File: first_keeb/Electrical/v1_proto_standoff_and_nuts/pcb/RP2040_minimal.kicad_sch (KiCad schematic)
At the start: 75 parts, among them J1 Conn_01x04_Socket, J2 Conn_01x04_Socket, P1 USB-TYPE-C-016, Q1 SN74LV1T34DBV, SW1 SK-3296S-01-L3, SW2 MS-22C01-G010, SW3 TS-1187A-B-A-B, SW4 MS-22C01-G010, SW5 TS-1187A-B-A-B, SW6 BUTT1, SW7 BUTT3, SW8 BUTT2, U1 AMS1117-2.5, U2 ME6208A44M3G, U3 PRTR5V0U2X, U4 MCP6001-OT, U5 STM32F401RCTx, U6 MCP6001-OT, U7 SLSS49E, U8 SLSS49E, U9 SLSS49E, Y1 8MHz

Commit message: - no more tan caps - adds 1u before ferrite - ties ties other side of boot0 resistor to gnd
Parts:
- removed J2: Conn_01x04_Socket, Connector_PinSocket_2.54mm:PinSocket_1x04_P2.54mm_Vertical, symbol Connector:Conn_01x04_Socket
- added C1: 1u, Capacitor_SMD:C_0402_1005Metric, symbol Device:C_Small
- C10: renamed from C9; value 10u -> 22u
- C11: renamed from C10; value 10u -> 22u
- C12: renamed from C11; value 10u -> 22u
- C13: renamed from C12; value 10u -> 22u
- C17: renamed from C16; value 4.7u -> 4u7
- U1: value AMS1117-2.5 -> ME6206A25XG; footprint Package_TO_SOT_SMD:SOT-223-3_TabPin2 -> Package_TO_SOT_SMD:SOT-23
- U2: footprint Package_TO_SOT_SMD:SOT-23 -> Package_TO_SOT_SMD:SOT-23-3
- renumbered C13 to C14, C14 to C15, C15 to C16, C17 to C18, C18 to C19, C1 to C2, C19 to C20, C20 to C21, C21 to C22, C22 to C23, C23 to C24, C24 to C25, C25 to C26, C26 to C27, C27 to C28, C28 to C29, C2 to C3, C29 to C30, C30 to C31, C31 to C32, C32 to C33, C3 to C4, C4 to C5, C5 to C6, C6 to C7, C7 to C8, C8 to C9
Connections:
- net BOOT0: now also R3.1, SW3.1; no longer R3.2
- net GND: now also R3.2, C1.2
- net VDD: now also C1.1
- net USART1_RX: no longer names the net of U5.59 (PB7)
- net USART1_TX: no longer names the net of U5.58 (PB6)
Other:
- note removed: "4.7u ceramic capacitor must be connected to one of the VDD pins"
- note removed: "Reccomend tantalum cap for improved stability on power supplies. To be cost effective, put the tantalum caps on MCU power first since the ADC uses that as its VREF and that requires more stability than the sensors"
- moved on the sheet: C2, C3, C4, C5, C6, C7, C8, C9, FB1, R3, R4

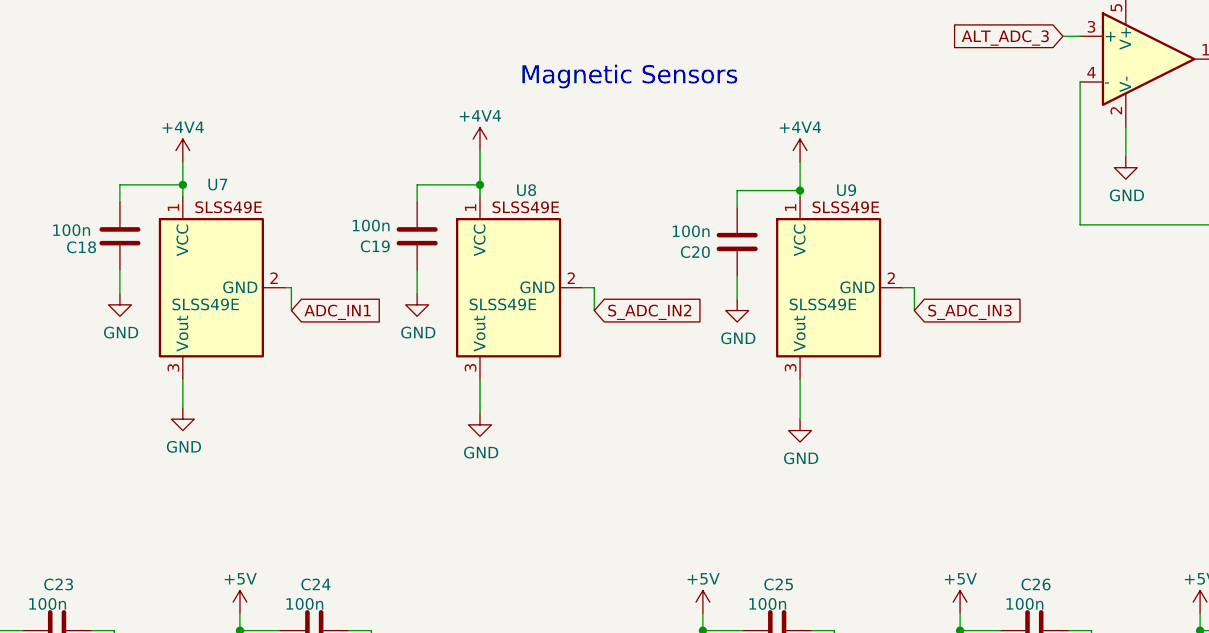
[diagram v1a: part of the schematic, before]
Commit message: fix mag sensor schematic
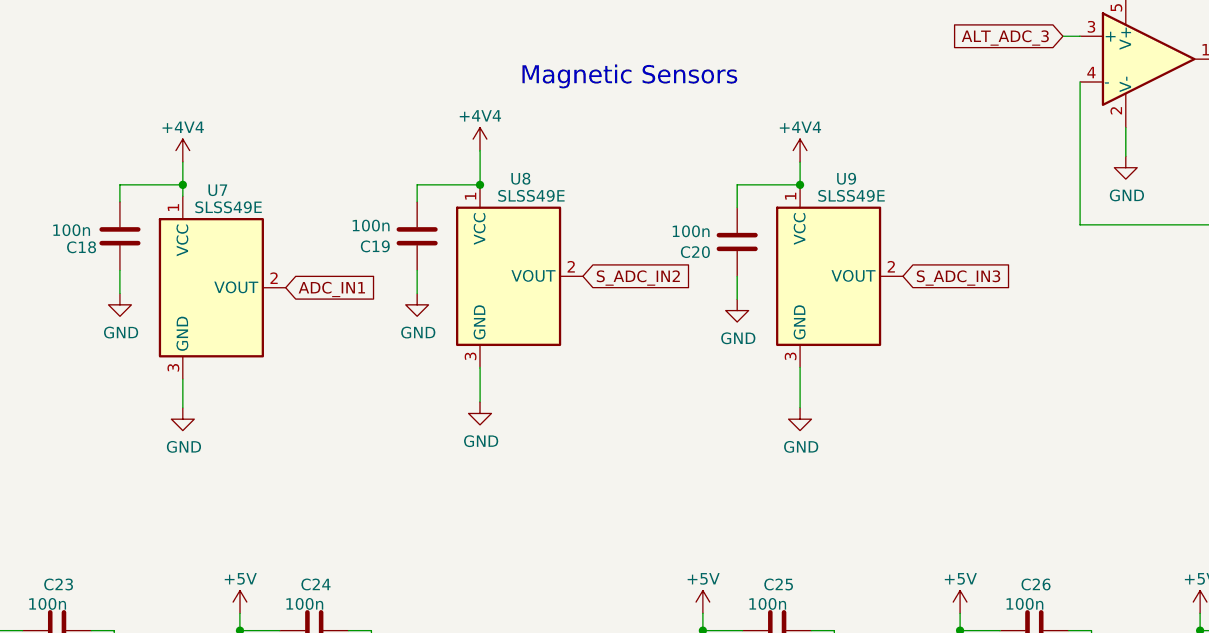
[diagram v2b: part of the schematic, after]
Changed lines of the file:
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@@
   (junction (at 236.22 46.355) (diameter 0) (color 0 0 0 0)
   )
-  (junction (at 330.2 167.64) (diameter 0) (color 0 0 0 0)
-  )
   (junction (at 101.6 40.64) (diameter 0) (color 0 0 0 0)
   )
@@
   (junction (at 73.025 40.64) (diameter 0) (color 0 0 0 0)
   )
+  (junction (at 330.2 167.005) (diameter 0) (color 0 0 0 0)
+  )
   (junction (at 41.275 66.04) (diameter 0) (color 0 0 0 0)
   )
@@
     (stroke (width 0) (type default))
   )
-  (wire (pts (xy 330.2 167.64) (xy 323.215 167.64))
-    (stroke (width 0) (type default))
-  )
   (wire (pts (xy 361.315 171.45) (xy 361.315 155.575))
     (stroke (width 0) (type default))
@@
     (stroke (width 0) (type default))
   )
-  (wire (pts (xy 273.05 178.435) (xy 273.685 178.435))
-    (stroke (width 0) (type default))
-  )
   (wire (pts (xy 228.6 134.62) (xy 228.6 133.985))
     (stroke (width 0) (type default))
@@
     (stroke (width 0) (type default))
   )
+  (wire (pts (xy 261.62 168.275) (xy 261.62 167.005))
+    (stroke (width 0) (type default))
+  )
   (wire (pts (xy 278.13 251.46) (xy 278.13 253.365))
     (stroke (width 0) (type default))
@@
     (stroke (width 0) (type default))
   )
+  (wire (pts (xy 330.2 164.465) (xy 330.2 167.005))
+    (stroke (width 0) (type default))
+  )
   (wire (pts (xy 292.735 253.365) (xy 290.195 253.365))
     (stroke (width 0) (type default))
@@
     (stroke (width 0) (type default))
   )
-  (wire (pts (xy 330.2 167.64) (xy 330.2 168.275))
-    (stroke (width 0) (type default))
-  )
   (wire (pts (xy 222.25 128.905) (xy 222.25 134.62))
     (stroke (width 0) (type default))
@@
     (stroke (width 0) (type default))
   )
-  (wire (pts (xy 294.64 188.595) (xy 294.64 192.405))
+  (wire (pts (xy 294.64 187.325) (xy 294.64 191.135))
     (stroke (width 0) (type default))
   )
@@
     (stroke (width 0) (type default))
   )
+  (wire (pts (xy 323.215 167.005) (xy 330.2 167.005))
+    (stroke (width 0) (type default))
+  )
   (wire (pts (xy 337.82 50.8) (xy 337.82 49.53))
     (stroke (width 0) (type default))
@@
     (stroke (width 0) (type default))
   )
-  (wire (pts (xy 306.07 178.435) (xy 307.34 178.435))
-    (stroke (width 0) (type default))
-  )
   (wire (pts (xy 282.575 216.535) (xy 280.035 216.535))
     (stroke (width 0) (type default))
@@
     (stroke (width 0) (type default))
   )
-  (wire (pts (xy 307.34 178.435) (xy 307.34 180.975))
-    (stroke (width 0) (type default))
-  )
   (wire (pts (xy 366.395 160.655) (xy 366.395 163.83))
     (stroke (width 0) (type default))
@@
     (stroke (width 0) (type default))
   )
-  (wire (pts (xy 273.685 178.435) (xy 273.685 180.975))
-    (stroke (width 0) (type default))
-  )
   (wire (pts (xy 78.74 65.405) (xy 78.74 66.675))
     (stroke (width 0) (type default))
@@
     (stroke (width 0) (type default))
   )
-  (wire (pts (xy 261.62 167.005) (xy 261.62 168.275))
-    (stroke (width 0) (type default))
-  )
-  (wire (pts (xy 342.9 180.975) (xy 342.9 178.435))
-    (stroke (width 0) (type default))
-  )
   (wire (pts (xy 149.86 100.33) (xy 150.495 100.33))
     (stroke (width 0) (type default))
@@
     (stroke (width 0) (type default))
   )
-  (wire (pts (xy 342.9 178.435) (xy 341.63 178.435))
-    (stroke (width 0) (type default))
-  )
   (wire (pts (xy 73.66 65.405) (xy 76.2 65.405))
     (stroke (width 0) (type default))
@@
     (stroke (width 0) (type default))
   )
-  (wire (pts (xy 330.2 164.465) (xy 330.2 167.64))
-    (stroke (width 0) (type default))
-  )
   (wire (pts (xy 361.95 125.73) (xy 361.95 113.03))
     (stroke (width 0) (type default))
@@
     (stroke (width 0) (type default))
   )
-  (wire (pts (xy 294.64 167.005) (xy 294.64 168.275))
-    (stroke (width 0) (type default))
-  )
-  (wire (pts (xy 330.2 188.595) (xy 330.2 193.04))
+  (wire (pts (xy 330.2 187.325) (xy 330.2 191.77))
     (stroke (width 0) (type default))
   )
@@
     (stroke (width 0) (type default))
   )
-  (wire (pts (xy 323.215 167.64) (xy 323.215 169.545))
+  (wire (pts (xy 323.215 167.005) (xy 323.215 169.545))
     (stroke (width 0) (type default))
   )
@@
     )
   )
-  (global_label "S_ADC_IN3" (shape input) (at 342.9 180.975 0) (fields_autoplaced)
+  (global_label "S_ADC_IN3" (shape input) (at 341.63 177.165 0) (fields_autoplaced)
     (effects (font (size 1.27 1.27)) (justify left))
-    (property "Intersheetrefs" "${INTERSHEET_REFS}" (at 355.0697 180.975 0)
+    (property "Intersheetrefs" "${INTERSHEET_REFS}" (at 353.7997 177.165 0)
       (effects (font (size 1.27 1.27)) (justify left) hide)
     )
@@
     )
   )
-  (global_label "ADC_IN1" (shape input) (at 273.685 180.975 0) (fields_autoplaced)
+  (global_label "ADC_IN1" (shape input) (at 273.05 178.435 0) (fields_autoplaced)
     (effects (font (size 1.27 1.27)) (justify left))
-    (property "Intersheetrefs" "${INTERSHEET_REFS}" (at 283.6776 180.975 0)
+    (property "Intersheetrefs" "${INTERSHEET_REFS}" (at 283.0426 178.435 0)
       (effects (font (size 1.27 1.27)) (justify left) hide)
     )
@@
     )
   )
-  (global_label "S_ADC_IN2" (shape input) (at 307.34 180.975 0) (fields_autoplaced)
+  (global_label "S_ADC_IN2" (shape input) (at 306.07 177.165 0) (fields_autoplaced)
     (effects (font (size 1.27 1.27)) (justify left))
-    (property "Intersheetrefs" "${INTERSHEET_REFS}" (at 319.5097 180.975 0)
+    (property "Intersheetrefs" "${INTERSHEET_REFS}" (at 318.2397 177.165 0)
       (effects (font (size 1.27 1.27)) (justify left) hide)
     )
@@
     )
   )
-  (symbol (lib_id "power:GND") (at 294.64 192.405 0) (unit 1)
+  (symbol (lib_id "power:GND") (at 294.64 191.135 0) (unit 1)
     (in_bom yes) (on_board yes) (dnp no)
-    (property "Reference" "#PWR043" (at 294.64 198.755 0)
+    (property "Reference" "#PWR043" (at 294.64 197.485 0)
       (effects (font (size 1.27 1.27)) hide)
     )
-    (property "Value" "GND" (at 294.767 196.7992 0)
+    (property "Value" "GND" (at 294.767 195.5292 0)
       (effects (font (size 1.27 1.27)))
     )
-    (property "Footprint" "" (at 294.64 192.405 0)
+    (property "Footprint" "" (at 294.64 191.135 0)
       (effects (font (size 1.27 1.27)) hide)
     )
-    (property "Datasheet" "" (at 294.64 192.405 0)
+    (property "Datasheet" "" (at 294.64 191.135 0)
       (effects (font (size 1.27 1.27)) hide)
     )
@@
     )
   )
-  (symbol (lib_id "power:GND") (at 330.2 193.04 0) (unit 1)
+  (symbol (lib_id "power:GND") (at 330.2 191.77 0) (unit 1)
     (in_bom yes) (on_board yes) (dnp no)
-    (property "Reference" "#PWR044" (at 330.2 199.39 0)
+    (property "Reference" "#PWR044" (at 330.2 198.12 0)
       (effects (font (size 1.27 1.27)) hide)
     )
-    (property "Value" "GND" (at 330.327 197.4342 0)
+    (property "Value" "GND" (at 330.327 196.1642 0)
       (effects (font (size 1.27 1.27)))
     )
-    (property "Footprint" "" (at 330.2 193.04 0)
+    (property "Footprint" "" (at 330.2 191.77 0)
       (effects (font (size 1.27 1.27)) hide)
     )
-    (property "Datasheet" "" (at 330.2 193.04 0)
+    (property "Datasheet" "" (at 330.2 191.77 0)
       (effects (font (size 1.27 1.27)) hide)
     )
@@
   (symbol (lib_id "Sensor_Magnetic:SLSS49E") (at 334.01 177.165 0) (unit 1)
     (in_bom yes) (on_board yes) (dnp no)
-    (property "Reference" "U9" (at 336.55 167.64 0)
+    (property "Reference" "U9" (at 336.55 166.37 0)
       (effects (font (size 1.27 1.27)) (justify right))
     )
-    (property "Value" "SLSS49E" (at 332.74 180.34 0)
+    (property "Value" "SLSS49E" (at 335.915 168.275 0)
       (effects (font (size 1.27 1.27)))
     )
@@
   (symbol (lib_id "Sensor_Magnetic:SLSS49E") (at 298.45 177.165 0) (unit 1)
     (in_bom yes) (on_board yes) (dnp no)
-    (property "Reference" "U8" (at 300.99 167.64 0)
+    (property "Reference" "U8" (at 300.355 166.37 0)
       (effects (font (size 1.27 1.27)) (justify right))
     )
-    (property "Value" "SLSS49E" (at 297.18 180.34 0)
+    (property "Value" "SLSS49E" (at 300.355 168.275 0)
       (effects (font (size 1.27 1.27)))
     )
@@
     )
   )
-  (symbol (lib_id "Sensor_Magnetic:SLSS49E") (at 265.43 177.165 0) (unit 1)
+  (symbol (lib_id "Sensor_Magnetic:SLSS49E") (at 265.43 178.435 0) (unit 1)
     (in_bom yes) (on_board yes) (dnp no)
-    (property "Reference" "U7" (at 266.7 167.005 0)
+    (property "Reference" "U7" (at 266.7 167.64 0)
       (effects (font (size 1.27 1.27)) (justify right))
     )
-    (property "Value" "SLSS49E" (at 264.16 180.34 0)
+    (property "Value" "SLSS49E" (at 266.7 169.545 0)
       (effects (font (size 1.27 1.27)))
     )
-    (property "Footprint" "Package_TO_SOT_SMD:SOT-23" (at 264.16 178.435 0)
+    (property "Footprint" "Package_TO_SOT_SMD:SOT-23" (at 264.16 179.705 0)
       (effects (font (size 1.27 1.27)) hide)
     )
-    (property "Datasheet" "" (at 264.16 178.435 0)
+    (property "Datasheet" "" (at 264.16 179.705 0)
       (effects (font (size 1.27 1.27)) hide)
     )

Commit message: add svg
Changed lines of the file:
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@@
-    (stroke (width 0) (type default))
-  )
-  (wire (pts (xy 393.7 245.11) (xy 287.655 245.11))
     (stroke (width 0) (type default))
   )
@@
     (stroke (width 0) (type default))
   )
-  (wire (pts (xy 393.7 226.06) (xy 393.7 245.11))
+  (wire (pts (xy 393.7 226.06) (xy 393.7 243.84))
     (stroke (width 0) (type default))
   )
@@
     (stroke (width 0) (type default))
   )
-  (wire (pts (xy 287.655 241.3) (xy 287.655 245.11))
-    (stroke (width 0) (type default))
-  )
   (wire (pts (xy 313.69 92.71) (xy 314.96 92.71))
     (stroke (width 0) (type default))
@@
     (stroke (width 0) (type default))
   )
-  (wire (pts (xy 128.905 241.3) (xy 128.905 262.89))
+  (wire (pts (xy 128.905 243.84) (xy 128.905 262.89))
     (stroke (width 0) (type default))
   )
@@
     (stroke (width 0) (type default))
   )
-  (wire (pts (xy 128.905 241.3) (xy 287.655 241.3))
-    (stroke (width 0) (type default))
-  )
+  (wire (pts (xy 128.905 243.84) (xy 393.7 243.84))
+    (stroke (width 0) (type default))
+  )
